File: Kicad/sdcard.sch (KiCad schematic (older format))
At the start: 4 parts, among them J701 SD_Card

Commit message: Added some part numbers.
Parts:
- J701: Digikey (none) -> 478-4059-1-ND; MPN (none) -> 145638009211859+; Manufacturer (none) -> Kyocera
- RN701: Digikey (none) -> 4609X-101-103LF-ND; MPN (none) -> 4609X-101-103LF; Manufacturer (none) -> Bourns
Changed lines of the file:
@@
 F 3 "http://portal.fciconnect.com/Comergent//fci/drawing/10067847.pdf" H 5950 3750 50  0001 C CNN
 F 4 "0" H 5950 3750 50  0001 C CNN "DNP"
+F 5 "478-4059-1-ND" H 5950 3750 50  0001 C CNN "Digikey"
+F 6 "145638009211859+" H 5950 3750 50  0001 C CNN "MPN"
+F 7 "Kyocera" H 5950 3750 50  0001 C CNN "Manufacturer"
 	1    5950 3750
 	1    0    0    -1
@@
 F 3 "http://www.vishay.com/docs/31509/csc.pdf" H 4300 2500 50  0001 C CNN
 F 4 "0" H 4300 2500 50  0001 C CNN "DNP"
+F 5 "4609X-101-103LF-ND" H 4300 2500 50  0001 C CNN "Digikey"
+F 6 "4609X-101-103LF" H 4300 2500 50  0001 C CNN "MPN"
+F 7 "Bourns" H 4300 2500 50  0001 C CNN "Manufacturer"
 	1    4300 2500
 	1    0    0    -1

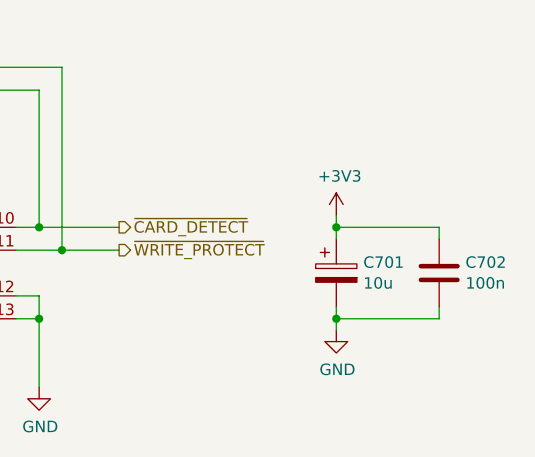
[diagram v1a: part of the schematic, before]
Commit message: Switch some of the radial THT Electrolytic caps for SMD MLCCs.
Also changed the STM32 for an LQFP-32 as it has a bigger pitch on the
pins.

The LQFP is easier to solder than the TSSOP, and the MLCC takes are
cheaper and take up less space.
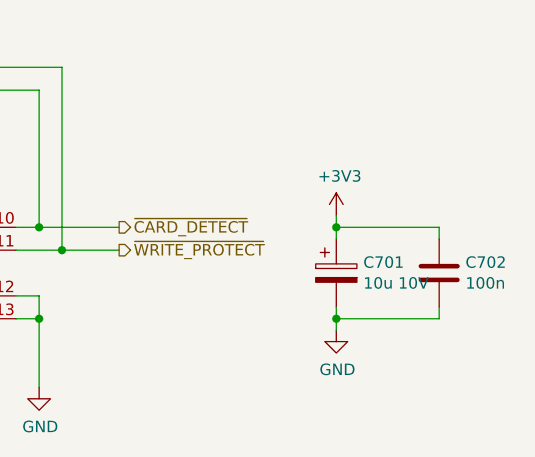
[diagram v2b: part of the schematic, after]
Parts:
- C701: value 10u -> 10u 10V; footprint Capacitor_THT:CP_Radial_D6.3mm_P2.50mm -> Capacitor_SMD:C_0805_2012Metric_Pad1.15x1.40mm_HandSolder; Digikey 493-10359-1-ND -> 1276-6455-1-ND; MPN UMW1E100MDD1TP -> CL21A106KOQNNNG; Manufacturer Nichicon -> Samsung
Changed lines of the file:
@@
 P 8250 3750
 F 0 "C701" H 8368 3796 50  0000 L CNN
-F 1 "10u" H 8368 3705 50  0000 L CNN
-F 2 "Capacitor_THT:CP_Radial_D6.3mm_P2.50mm" H 8288 3600 50  0001 C CNN
+F 1 "10u 10V" H 8368 3705 50  0000 L CNN
+F 2 "Capacitor_SMD:C_0805_2012Metric_Pad1.15x1.40mm_HandSolder" H 8288 3600 50  0001 C CNN
 F 3 "~" H 8250 3750 50  0001 C CNN
 F 4 "0" H 8250 3750 50  0001 C CNN "DNP"
-F 5 "493-10359-1-ND" H 8250 3750 50  0001 C CNN "Digikey"
-F 6 "UMW1E100MDD1TP" H 8250 3750 50  0001 C CNN "MPN"
-F 7 "Nichicon" H 8250 3750 50  0001 C CNN "Manufacturer"
+F 5 "1276-6455-1-ND" H 8250 3750 50  0001 C CNN "Digikey"
+F 6 "CL21A106KOQNNNG" H 8250 3750 50  0001 C CNN "MPN"
+F 7 "Samsung" H 8250 3750 50  0001 C CNN "Manufacturer"
 	1    8250 3750
 	1    0    0    -1

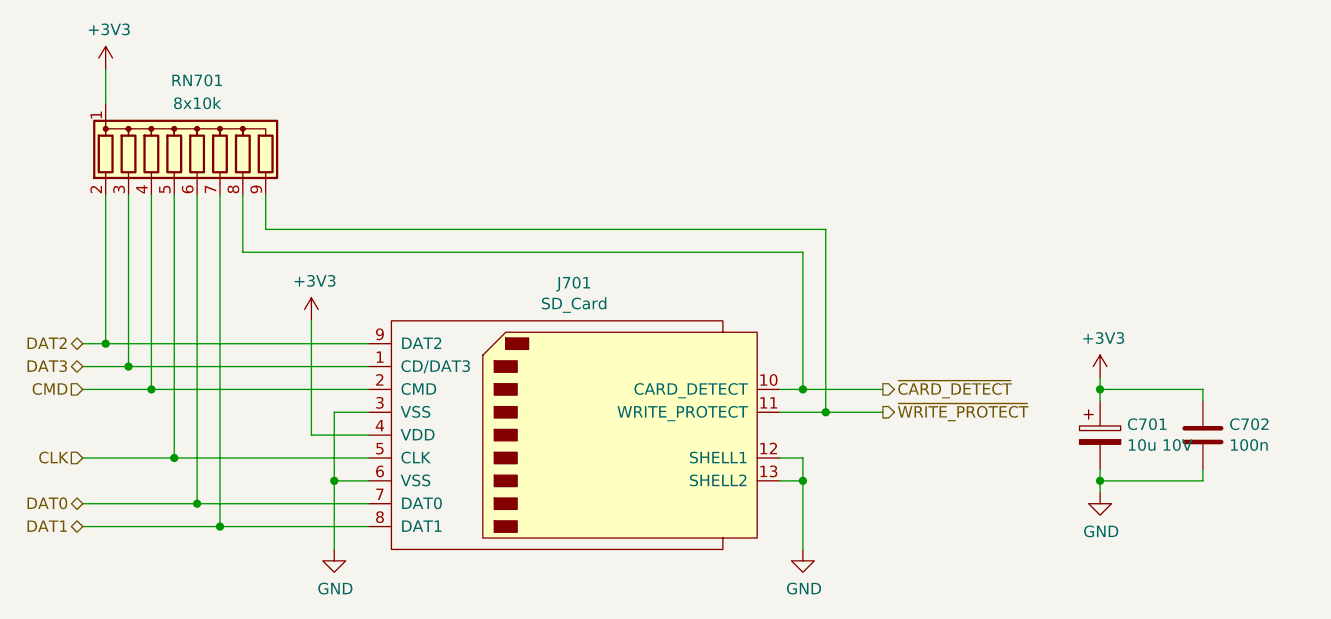
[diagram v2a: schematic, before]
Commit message: Added 12-bit video DAC.
Also had to change footprints to suit Kicad 5.1.9
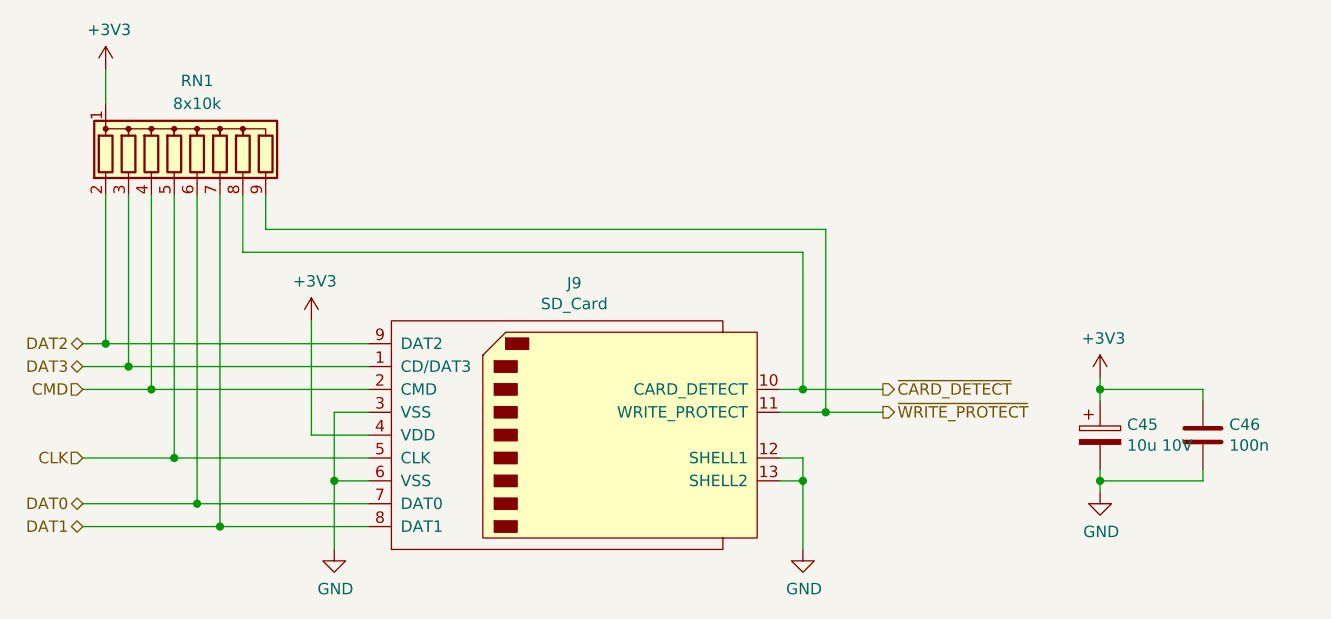
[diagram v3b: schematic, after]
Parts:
- C45: renamed from C701; footprint Capacitor_SMD:C_0805_2012Metric_Pad1.15x1.40mm_HandSolder -> Capacitor_SMD:C_0805_2012Metric_Pad1.18x1.45mm_HandSolder
- C46: renamed from C702; footprint Capacitor_SMD:C_0805_2012Metric_Pad1.15x1.40mm_HandSolder -> Capacitor_SMD:C_0805_2012Metric_Pad1.18x1.45mm_HandSolder
- renumbered J701 to J9, RN701 to RN1
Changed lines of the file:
@@
 $Descr A4 11693 8268
 encoding utf-8
-Sheet 4 12
+Sheet 7 16
 Title "Neotron Common Hardware - SD Card Slot"
 Date "2021-01-01"
@@
 $EndDescr
 $Comp
-L Connector:SD_Card J701
+L Connector:SD_Card J9
 U 1 1 5FE7BB6E
 P 5950 3750
-F 0 "J701" H 5950 4415 50  0000 C CNN
+F 0 "J9" H 5950 4415 50  0000 C CNN
 F 1 "SD_Card" H 5950 4324 50  0000 C CNN
 F 2 "Connector_Card:SD_Kyocera_145638009211859+" H 5950 3750 50  0001 C CNN
@@
 DAT1
 $Comp
-L power:+3V3 #PWR0702
+L power:+3V3 #PWR0108
 U 1 1 5FE7CAA7
 P 4800 3250
-F 0 "#PWR0702" H 4800 3100 50  0001 C CNN
+F 0 "#PWR0108" H 4800 3100 50  0001 C CNN
 F 1 "+3V3" H 4815 3423 50  0000 C CNN
 F 2 "" H 4800 3250 50  0001 C CNN
@@
 	4800 3750 4800 3250
 $Comp
-L power:GND #PWR0705
+L power:GND #PWR0109
 U 1 1 5FE7D47D
 P 4900 4250
-F 0 "#PWR0705" H 4900 4000 50  0001 C CNN
+F 0 "#PWR0109" H 4900 4000 50  0001 C CNN
 F 1 "GND" H 4905 4077 50  0000 C CNN
 F 2 "" H 4900 4250 50  0001 C CNN
@@
 	4400 4150 3800 4150
 $Comp
-L power:+3V3 #PWR0701
+L power:+3V3 #PWR0107
 U 1 1 5FE8424F
 P 3900 2150
-F 0 "#PWR0701" H 3900 2000 50  0001 C CNN
+F 0 "#PWR0107" H 3900 2000 50  0001 C CNN
 F 1 "+3V3" H 3915 2323 50  0000 C CNN
 F 2 "" H 3900 2150 50  0001 C CNN
@@
 	3900 2150 3900 2300
 $Comp
-L power:+3V3 #PWR0703
+L power:+3V3 #PWR0111
 U 1 1 5FE84AEC
 P 8250 3500
-F 0 "#PWR0703" H 8250 3350 50  0001 C CNN
+F 0 "#PWR0111" H 8250 3350 50  0001 C CNN
 F 1 "+3V3" H 8265 3673 50  0000 C CNN
 F 2 "" H 8250 3500 50  0001 C CNN
@@
 $EndComp
 $Comp
-L power:GND #PWR0704
+L power:GND #PWR0112
 U 1 1 5FE84E43
 P 8250 4000
-F 0 "#PWR0704" H 8250 3750 50  0001 C CNN
+F 0 "#PWR0112" H 8250 3750 50  0001 C CNN
 F 1 "GND" H 8255 3827 50  0000 C CNN
 F 2 "" H 8250 4000 50  0001 C CNN
@@
 $EndComp
 $Comp
-L Device:CP C701
+L Device:CP C45
 U 1 1 5FE85358
 P 8250 3750
-F 0 "C701" H 8368 3796 50  0000 L CNN
+F 0 "C45" H 8368 3796 50  0000 L CNN
 F 1 "10u 10V" H 8368 3705 50  0000 L CNN
-F 2 "Capacitor_SMD:C_0805_2012Metric_Pad1.15x1.40mm_HandSolder" H 8288 3600 50  0001 C CNN
+F 2 "Capacitor_SMD:C_0805_2012Metric_Pad1.18x1.45mm_HandSolder" H 8288 3600 50  0001 C CNN
 F 3 "~" H 8250 3750 50  0001 C CNN
 F 4 "0" H 8250 3750 50  0001 C CNN "DNP"
@@
 $EndComp
 $Comp
-L Device:C C702
+L Device:C C46
 U 1 1 5FE86138
 P 8700 3750
-F 0 "C702" H 8815 3796 50  0000 L CNN
+F 0 "C46" H 8815 3796 50  0000 L CNN
 F 1 "100n" H 8815 3705 50  0000 L CNN
-F 2 "Capacitor_SMD:C_0805_2012Metric_Pad1.15x1.40mm_HandSolder" H 8738 3600 50  0001 C CNN
+F 2 "Capacitor_SMD:C_0805_2012Metric_Pad1.18x1.45mm_HandSolder" H 8738 3600 50  0001 C CNN
 F 3 "~" H 8700 3750 50  0001 C CNN
 F 4 "0" H 8700 3750 50  0001 C CNN "DNP"
@@
 Connection ~ 8250 3950
 $Comp
-L power:GND #PWR0706
+L power:GND #PWR0110
 U 1 1 5FE89E21
 P 6950 4250
-F 0 "#PWR0706" H 6950 4000 50  0001 C CNN
+F 0 "#PWR0110" H 6950 4000 50  0001 C CNN
 F 1 "GND" H 6955 4077 50  0000 C CNN
 F 2 "" H 6950 4250 50  0001 C CNN
@@
 ~WRITE_PROTECT
 $Comp
-L Device:R_Network08 RN701
+L Device:R_Network08 RN1
 U 1 1 5FE7DE1F
 P 4300 2500
-F 0 "RN701" H 4300 2800 50  0000 C CNN
+F 0 "RN1" H 4300 2800 50  0000 C CNN
 F 1 "8x10k" H 4300 2700 50  0000 C CNN
 F 2 "Resistor_THT:R_Array_SIP9" V 4675 2500 50  0001 C CNN

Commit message: Add 4-bit Video DAC, and re-wire BMC.
Now the BMC is an SPI device, and has a four-wire UART.
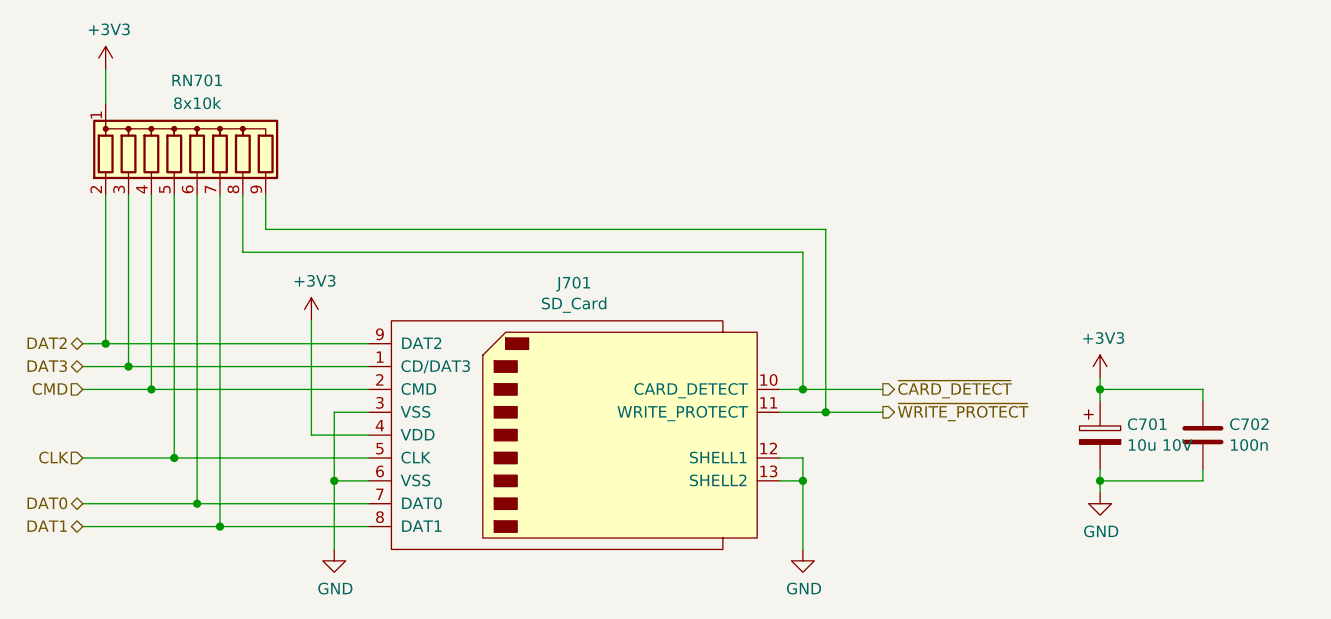
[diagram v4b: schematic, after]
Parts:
- renumbered C45 to C701, C46 to C702, J9 to J701, RN1 to RN701
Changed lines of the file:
@@
 Sheet 7 16
 Title "Neotron Common Hardware - SD Card Slot"
-Date "2021-01-01"
+Date "2021-04-02"
 Rev "[Uncontrolled]"
 Comp "https://neotron-compute.github.io/"
@@
 $EndDescr
 $Comp
-L Connector:SD_Card J9
+L Connector:SD_Card J701
 U 1 1 5FE7BB6E
 P 5950 3750
-F 0 "J9" H 5950 4415 50  0000 C CNN
+F 0 "J701" H 5950 4415 50  0000 C CNN
 F 1 "SD_Card" H 5950 4324 50  0000 C CNN
 F 2 "Connector_Card:SD_Kyocera_145638009211859+" H 5950 3750 50  0001 C CNN
@@
 DAT1
 $Comp
-L power:+3V3 #PWR0108
+L power:+3V3 #PWR0702
 U 1 1 5FE7CAA7
 P 4800 3250
-F 0 "#PWR0108" H 4800 3100 50  0001 C CNN
+F 0 "#PWR0702" H 4800 3100 50  0001 C CNN
 F 1 "+3V3" H 4815 3423 50  0000 C CNN
 F 2 "" H 4800 3250 50  0001 C CNN
@@
 	4800 3750 4800 3250
 $Comp
-L power:GND #PWR0109
+L power:GND #PWR0703
 U 1 1 5FE7D47D
 P 4900 4250
-F 0 "#PWR0109" H 4900 4000 50  0001 C CNN
+F 0 "#PWR0703" H 4900 4000 50  0001 C CNN
 F 1 "GND" H 4905 4077 50  0000 C CNN
 F 2 "" H 4900 4250 50  0001 C CNN
@@
 	4400 4150 3800 4150
 $Comp
-L power:+3V3 #PWR0107
+L power:+3V3 #PWR0701
 U 1 1 5FE8424F
 P 3900 2150
-F 0 "#PWR0107" H 3900 2000 50  0001 C CNN
+F 0 "#PWR0701" H 3900 2000 50  0001 C CNN
 F 1 "+3V3" H 3915 2323 50  0000 C CNN
 F 2 "" H 3900 2150 50  0001 C CNN
@@
 	3900 2150 3900 2300
 $Comp
-L power:+3V3 #PWR0111
+L power:+3V3 #PWR0705
 U 1 1 5FE84AEC
 P 8250 3500
-F 0 "#PWR0111" H 8250 3350 50  0001 C CNN
+F 0 "#PWR0705" H 8250 3350 50  0001 C CNN
 F 1 "+3V3" H 8265 3673 50  0000 C CNN
 F 2 "" H 8250 3500 50  0001 C CNN
@@
 $EndComp
 $Comp
-L power:GND #PWR0112
+L power:GND #PWR0706
 U 1 1 5FE84E43
 P 8250 4000
-F 0 "#PWR0112" H 8250 3750 50  0001 C CNN
+F 0 "#PWR0706" H 8250 3750 50  0001 C CNN
 F 1 "GND" H 8255 3827 50  0000 C CNN
 F 2 "" H 8250 4000 50  0001 C CNN
@@
 $EndComp
 $Comp
-L Device:CP C45
+L Device:CP C701
 U 1 1 5FE85358
 P 8250 3750
-F 0 "C45" H 8368 3796 50  0000 L CNN
+F 0 "C701" H 8368 3796 50  0000 L CNN
 F 1 "10u 10V" H 8368 3705 50  0000 L CNN
 F 2 "Capacitor_SMD:C_0805_2012Metric_Pad1.18x1.45mm_HandSolder" H 8288 3600 50  0001 C CNN
@@
 $EndComp
 $Comp
-L Device:C C46
+L Device:C C702
 U 1 1 5FE86138
 P 8700 3750
-F 0 "C46" H 8815 3796 50  0000 L CNN
+F 0 "C702" H 8815 3796 50  0000 L CNN
 F 1 "100n" H 8815 3705 50  0000 L CNN
 F 2 "Capacitor_SMD:C_0805_2012Metric_Pad1.18x1.45mm_HandSolder" H 8738 3600 50  0001 C CNN
@@
 Connection ~ 8250 3950
 $Comp
-L power:GND #PWR0110
+L power:GND #PWR0704
 U 1 1 5FE89E21
 P 6950 4250
-F 0 "#PWR0110" H 6950 4000 50  0001 C CNN
+F 0 "#PWR0704" H 6950 4000 50  0001 C CNN
 F 1 "GND" H 6955 4077 50  0000 C CNN
 F 2 "" H 6950 4250 50  0001 C CNN
@@
 ~WRITE_PROTECT
 $Comp
-L Device:R_Network08 RN1
+L Device:R_Network08 RN701
 U 1 1 5FE7DE1F
 P 4300 2500
-F 0 "RN1" H 4300 2800 50  0000 C CNN
+F 0 "RN701" H 4300 2800 50  0000 C CNN
 F 1 "8x10k" H 4300 2700 50  0000 C CNN
 F 2 "Resistor_THT:R_Array_SIP9" V 4675 2500 50  0001 C CNN

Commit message: Tidy up part nos and swapped I2C/UART on BMC.
Mark all resistors as 1% if not specified.
Added some Mouser part numbers.
BMC can now be programmed over UART.
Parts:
- C702: Mouser (none) -> 594-K104K15X7RF5TL2
- J701: Mouser (none) -> 581-145638009211859+
- RN701: Mouser (none) -> 652-4609X-1LF-10K
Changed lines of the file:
@@
 F 6 "145638009211859+" H 5950 3750 50  0001 C CNN "MPN"
 F 7 "Kyocera" H 5950 3750 50  0001 C CNN "Manufacturer"
+F 8 "581-145638009211859+ " H 5950 3750 50  0001 C CNN "Mouser"
 	1    5950 3750
 	1    0    0    -1
@@
 F 6 "K104K15X7RF5TL2" H 8700 3750 50  0001 C CNN "MPN"
 F 7 "Vishay" H 8700 3750 50  0001 C CNN "Manufacturer"
+F 8 "594-K104K15X7RF5TL2" H 8700 3750 50  0001 C CNN "Mouser"
 	1    8700 3750
 	1    0    0    -1
@@
 F 6 "4609X-101-103LF" H 4300 2500 50  0001 C CNN "MPN"
 F 7 "Bourns" H 4300 2500 50  0001 C CNN "Manufacturer"
+F 8 "652-4609X-1LF-10K" H 4300 2500 50  0001 C CNN "Mouser"
 	1    4300 2500
 	1    0    0    -1

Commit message: Remove more errant spaces.
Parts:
- J701: Mouser 581-145638009211859+ -> 581-145638009211859+
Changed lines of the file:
@@
 F 6 "145638009211859+" H 5950 3750 50  0001 C CNN "MPN"
 F 7 "Kyocera" H 5950 3750 50  0001 C CNN "Manufacturer"
-F 8 "581-145638009211859+ " H 5950 3750 50  0001 C CNN "Mouser"
+F 8 "581-145638009211859+" H 5950 3750 50  0001 C CNN "Mouser"
 	1    5950 3750
 	1    0    0    -1

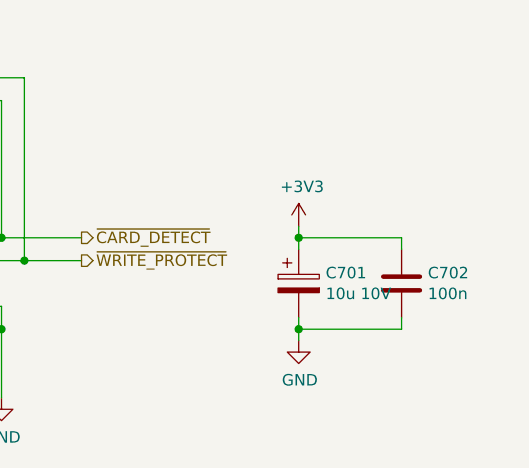
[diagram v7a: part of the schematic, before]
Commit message: Brought in sheets from Neotron Pico.
Also includes DB15HD and PSU 3D models.
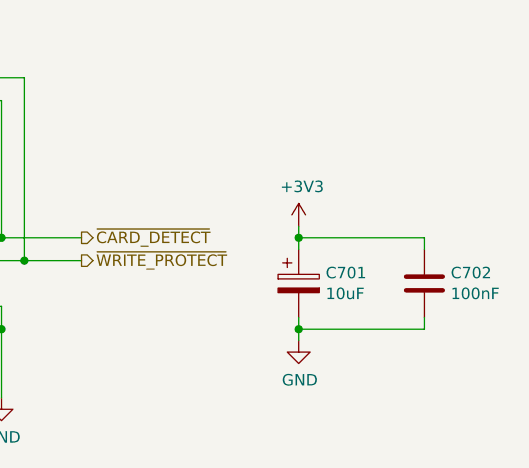
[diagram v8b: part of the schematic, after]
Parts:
- C701: value 10u 10V -> 10uF; Digikey 1276-6455-1-ND -> (none); LCSC Part# (none) -> C15850; MPN CL21A106KOQNNNG -> CPL-CAP-X5R-0805-10UF-16V; Manufacturer Samsung -> CPL
- C702: value 100n -> 100nF; Digikey BC1150CT-ND -> (none); LCSC Part# (none) -> C49678; MPN K104K15X7RF5TL2 -> CPL-CAP-X7R-0805-100NF-50V; Manufacturer Vishay -> CPL; Mouser 594-K104K15X7RF5TL2 -> (none)
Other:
- moved on the sheet: C702
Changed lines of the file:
@@
 $Descr A4 11693 8268
 encoding utf-8
-Sheet 7 17
-Title "Neotron Common Hardware - SD Card Slot"
-Date "2021-04-02"
+Sheet 7 18
+Title "Neotron Common Hardware"
+Date "2021-06-18"
 Rev "[Uncontrolled]"
 Comp "https://neotron-compute.github.io/"
@@
 F 7 "Kyocera" H 5950 3750 50  0001 C CNN "Manufacturer"
 F 8 "581-145638009211859+" H 5950 3750 50  0001 C CNN "Mouser"
+F 9 "~" H 5950 3750 50  0001 C CNN "LCSC Part#"
 	1    5950 3750
 	1    0    0    -1
@@
 P 8250 3750
 F 0 "C701" H 8368 3796 50  0000 L CNN
-F 1 "10u 10V" H 8368 3705 50  0000 L CNN
+F 1 "10uF" H 8368 3705 50  0000 L CNN
 F 2 "Capacitor_SMD:C_0805_2012Metric_Pad1.18x1.45mm_HandSolder" H 8288 3600 50  0001 C CNN
 F 3 "~" H 8250 3750 50  0001 C CNN
 F 4 "0" H 8250 3750 50  0001 C CNN "DNP"
-F 5 "1276-6455-1-ND" H 8250 3750 50  0001 C CNN "Digikey"
-F 6 "CL21A106KOQNNNG" H 8250 3750 50  0001 C CNN "MPN"
-F 7 "Samsung" H 8250 3750 50  0001 C CNN "Manufacturer"
+F 5 "" H 8250 3750 50  0001 C CNN "Digikey"
+F 6 "CPL-CAP-X5R-0805-10UF-16V" H 8250 3750 50  0001 C CNN "MPN"
+F 7 "CPL" H 8250 3750 50  0001 C CNN "Manufacturer"
+F 8 "C15850" H 8250 3750 50  0001 C CNN "LCSC Part#"
 	1    8250 3750
 	1    0    0    -1
@@
 L Device:C C702
 U 1 1 5FE86138
-P 8700 3750
-F 0 "C702" H 8815 3796 50  0000 L CNN
-F 1 "100n" H 8815 3705 50  0000 L CNN
-F 2 "Capacitor_SMD:C_0805_2012Metric_Pad1.18x1.45mm_HandSolder" H 8738 3600 50  0001 C CNN
-F 3 "~" H 8700 3750 50  0001 C CNN
-F 4 "0" H 8700 3750 50  0001 C CNN "DNP"
-F 5 "BC1150CT-ND" H 8700 3750 50  0001 C CNN "Digikey"
-F 6 "K104K15X7RF5TL2" H 8700 3750 50  0001 C CNN "MPN"
-F 7 "Vishay" H 8700 3750 50  0001 C CNN "Manufacturer"
-F 8 "594-K104K15X7RF5TL2" H 8700 3750 50  0001 C CNN "Mouser"
-	1    8700 3750
+P 8800 3750
+F 0 "C702" H 8915 3796 50  0000 L CNN
+F 1 "100nF" H 8915 3705 50  0000 L CNN
+F 2 "Capacitor_SMD:C_0805_2012Metric_Pad1.18x1.45mm_HandSolder" H 8838 3600 50  0001 C CNN
+F 3 "~" H 8800 3750 50  0001 C CNN
+F 4 "0" H 8800 3750 50  0001 C CNN "DNP"
+F 5 "" H 8800 3750 50  0001 C CNN "Digikey"
+F 6 "CPL-CAP-X7R-0805-100NF-50V" H 8800 3750 50  0001 C CNN "MPN"
+F 7 "CPL" H 8800 3750 50  0001 C CNN "Manufacturer"
+F 8 "" H 8800 3750 50  0001 C CNN "Mouser"
+F 9 "C49678" H 8800 3750 50  0001 C CNN "LCSC Part#"
+	1    8800 3750
 	1    0    0    -1
 $EndComp
@@
 	8250 3500 8250 3550
 Wire Wire Line
-	8250 3550 8700 3550
-Wire Wire Line
-	8700 3550 8700 3600
+	8250 3550 8800 3550
+Wire Wire Line
+	8800 3550 8800 3600
 Connection ~ 8250 3550
 Wire Wire Line
 	8250 3550 8250 3600
 Wire Wire Line
-	8700 3900 8700 3950
-Wire Wire Line
-	8700 3950 8250 3950
+	8800 3900 8800 3950
+Wire Wire Line
+	8800 3950 8250 3950
 Wire Wire Line
 	8250 3950 8250 3900
@@
 F 7 "Bourns" H 4300 2500 50  0001 C CNN "Manufacturer"
 F 8 "652-4609X-1LF-10K" H 4300 2500 50  0001 C CNN "Mouser"
+F 9 "~" H 4300 2500 50  0001 C CNN "LCSC Part#"
 	1    4300 2500
 	1    0    0    -1
